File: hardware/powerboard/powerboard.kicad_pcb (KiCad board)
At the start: 4 copper layers, 81.2 x 50.7 mm, 73 parts, among them J1 USB_B_Micro, J10 5V, J11 3V3, J2 Boot, J3 Keysboard Header, J4 Display, J5 Debug, J7 UART_0, J8 I2C_0, J9 I2C_1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

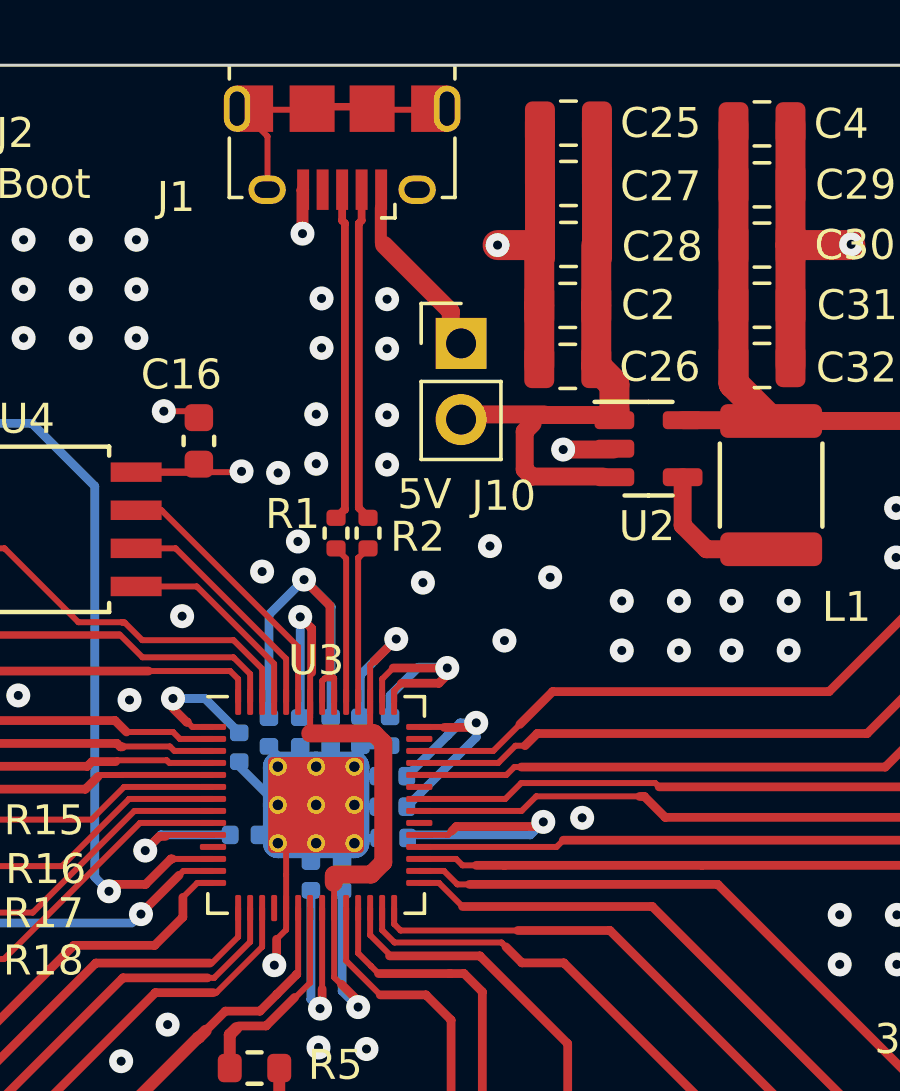
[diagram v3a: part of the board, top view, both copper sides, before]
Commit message: output file changes AND notes! Octave is now limited between 9 2 which corresponds to a piano range of C8 to C1, there are 3 notes below C1, that we will not be able to produce.
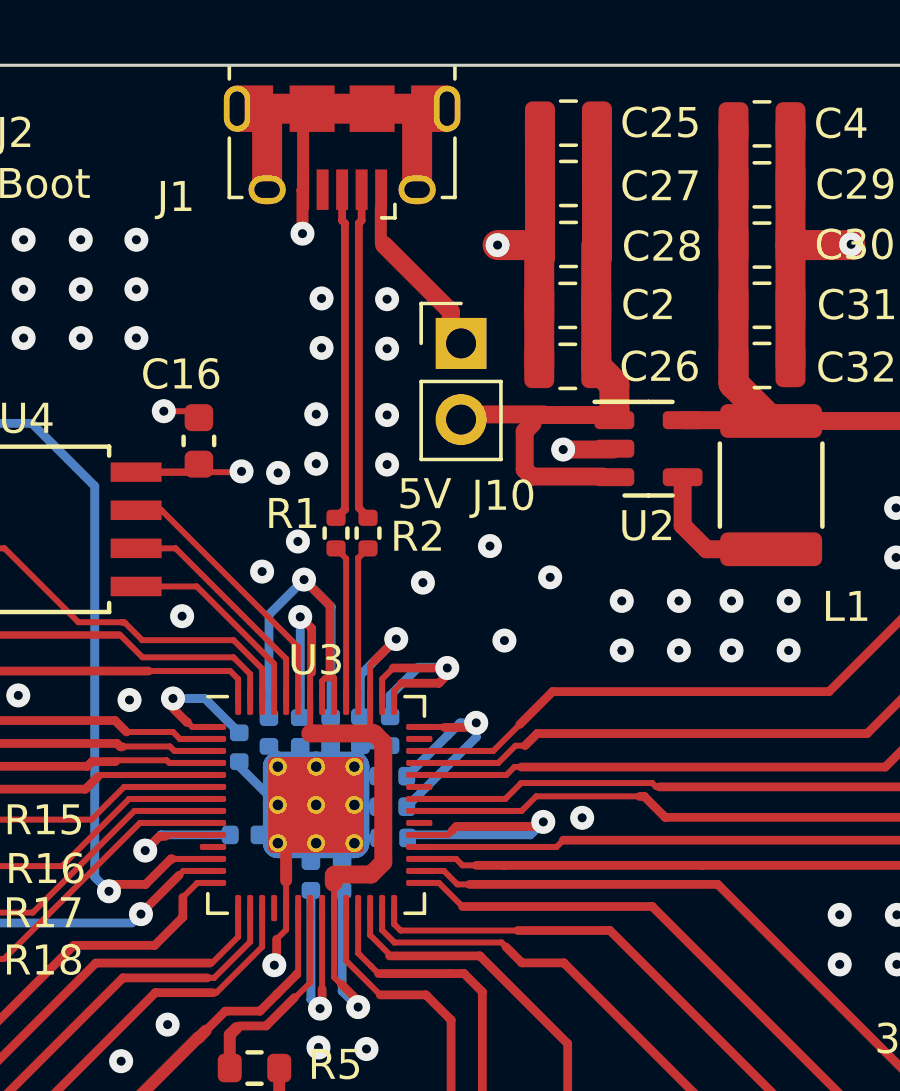
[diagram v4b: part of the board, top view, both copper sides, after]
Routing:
- net GND: track 105.7 -> 111.1 mm
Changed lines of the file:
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@@
     (effects (font (size 1 1) (thickness 0.15)))
   )
+  (segment (start 75.281 19.337) (end 75.281 16.937) (width 0.4) (layer "F.Cu") (net 1))
   (segment (start 58.6993 46.6344) (end 59.4613 47.3964) (width 0.2) (layer "F.Cu") (net 1))
+  (segment (start 75.581 16.637) (end 73.681 16.637) (width 1) (layer "F.Cu") (net 1))
   (segment (start 118.9494 37.374) (end 125.4494 37.374) (width 0.29337) (layer "F.Cu") (net 1))
   (segment (start 75.1722 53.6058) (end 75.184 53.594) (width 0.4) (layer "F.Cu") (net 1))
@@
   (segment (start 116.6244 56.1848) (end 116.6244 55.131) (width 0.29337) (layer "F.Cu") (net 1))
   (segment (start 99.5172 19.3294) (end 99.5172 19.203) (width 0.2) (layer "F.Cu") (net 1))
+  (segment (start 74.7144 43.28315) (end 74.7144 42.3672) (width 0.2) (layer "F.Cu") (net 1))
   (segment (start 83.17715 21.1632) (end 83.17715 19.1312) (width 1) (layer "F.Cu") (net 1))
   (segment (start 64.4652 32.4866) (end 64.389 32.5628) (width 0.2) (layer "F.Cu") (net 1))
@@
   (segment (start 74.3966 45.110004) (end 74.3458 45.160804) (width 0.29337) (layer "F.Cu") (net 1))
   (segment (start 58.2676 45.6184) (end 59.2581 45.6184) (width 0.2) (layer "F.Cu") (net 1))
+  (segment (start 74.081 17.037) (end 73.681 16.637) (width 1) (layer "F.Cu") (net 1))
   (segment (start 59.4613 44.2468) (end 58.6232 44.2468) (width 0.2) (layer "F.Cu") (net 1))
   (segment (start 75.2602 19.3528) (end 75.281 19.332) (width 0.4) (layer "F.Cu") (net 1))
-  (segment (start 74.7144 42.177) (end 74.7144 40.84565) (width 0.2) (layer "F.Cu") (net 1))
   (segment (start 74.7144 40.84565) (end 75.7144 39.84565) (width 0.2) (layer "F.Cu") (net 1))
-  (segment (start 77.731 16.672) (end 79.956 16.672) (width 0.2) (layer "F.Cu") (net 1))
+  (segment (start 74.7144 42.3672) (end 74.7144 40.84565) (width 0.4) (layer "F.Cu") (net 1))
   (segment (start 72.2884 50.2158) (end 72.263 50.2412) (width 0.4) (layer "F.Cu") (net 1))
   (segment (start 83.15175 21.1886) (end 83.17715 21.1632) (width 0.4) (layer "F.Cu") (net 1))
@@
   (segment (start 85.6285 27.99855) (end 85.65665 27.9704) (width 0.4) (layer "F.Cu") (net 1))
   (segment (start 74.3966 44.323) (end 74.7144 44.0052) (width 0.2) (layer "F.Cu") (net 1))
+  (segment (start 75.581 16.637) (end 77.581 16.637) (width 1) (layer "F.Cu") (net 1))
   (segment (start 125.7046 31.4452) (end 126.5454 31.4452) (width 0.25) (layer "F.Cu") (net 1))
   (segment (start 105.3084 29.6926) (end 105.3084 28.5978) (width 0.25) (layer "F.Cu") (net 1))
@@
   (segment (start 70.9552 51.5202) (end 70.9552 50.165) (width 0.4) (layer "F.Cu") (net 1))
   (segment (start 99.581 19.1392) (end 99.581 17.7292) (width 0.6) (layer "F.Cu") (net 1))
+  (segment (start 79.081 19.337) (end 79.081 17.037) (width 1) (layer "F.Cu") (net 1))
   (segment (start 74.3966 44.323) (end 74.3966 45.110004) (width 0.29337) (layer "F.Cu") (net 1))
   (segment (start 105.0798 20.574) (end 105.0798 21.183) (width 0.2) (layer "F.Cu") (net 1))
@@
   (segment (start 116.7006 38.6464) (end 116.7006 39.7002) (width 0.29337) (layer "F.Cu") (net 1))
   (segment (start 58.2422 43.4848) (end 58.6993 43.4848) (width 0.2) (layer "F.Cu") (net 1))
-  (segment (start 74.0935 19.247) (end 74.0935 17.5595) (width 0.2) (layer "F.Cu") (net 1))
   (segment (start 74.7144 44.0052) (end 74.7144 43.28315) (width 0.2) (layer "F.Cu") (net 1))
   (segment (start 75.2602 20.8026) (end 75.2602 19.3528) (width 0.4) (layer "F.Cu") (net 1))
   (segment (start 126.5454 31.4452) (end 127.0026 30.988) (width 0.25) (layer "F.Cu") (net 1))
   (segment (start 115.951 37.8968) (end 116.7006 38.6464) (width 0.29337) (layer "F.Cu") (net 1))
-  (segment (start 74.0935 17.5595) (end 73.206 16.672) (width 0.2) (layer "F.Cu") (net 1))
   (segment (start 83.15175 25.2272) (end 83.15175 23.1952) (width 1) (layer "F.Cu") (net 1))
   (segment (start 70.6374 26.7208) (end 71.9452 26.7208) (width 0.2) (layer "F.Cu") (net 1))
   (segment (start 116.6244 55.131) (end 116.1288 54.6354) (width 0.29337) (layer "F.Cu") (net 1))
-  (segment (start 75.581 16.572) (end 77.581 16.572) (width 0.25) (layer "F.Cu") (net 1))
+  (segment (start 77.581 16.637) (end 79.481 16.637) (width 1) (layer "F.Cu") (net 1))
   (segment (start 93.5228 21.1836) (end 93.5482 21.1582) (width 0.4) (layer "F.Cu") (net 1))
   (segment (start 85.60585 28.0212) (end 85.5832 27.99855) (width 0.4) (layer "F.Cu") (net 1))
@@
   (segment (start 71.3408 51.9058) (end 70.9552 51.5202) (width 0.4) (layer "F.Cu") (net 1))
   (segment (start 83.15175 23.1952) (end 83.15175 21.1886) (width 1) (layer "F.Cu") (net 1))
-  (segment (start 74.7144 43.28315) (end 74.7144 42.177) (width 0.2) (layer "F.Cu") (net 1))
   (segment (start 74.3458 45.160804) (end 74.320202 45.186402) (width 0.2) (layer "F.Cu") (net 1))
-  (segment (start 75.031 16.672) (end 73.206 16.672) (width 0.2) (layer "F.Cu") (net 1))
+  (segment (start 79.081 17.037) (end 79.481 16.637) (width 1) (layer "F.Cu") (net 1))
   (segment (start 99.5172 19.203) (end 99.581 19.1392) (width 0.2) (layer "F.Cu") (net 1))
+  (segment (start 75.281 16.937) (end 75.581 16.637) (width 0.4) (layer "F.Cu") (net 1))
   (segment (start 83.94935 27.99855) (end 85.6285 27.99855) (width 0.6) (layer "F.Cu") (net 1))
+  (segment (start 74.081 19.337) (end 74.081 17.037) (width 1) (layer "F.Cu") (net 1))
   (segment (start 83.1748 19.12885) (end 83.17715 19.1312) (width 0.4) (layer "F.Cu") (net 1))
   (segment (start 73.5408 53.6058) (end 75.1722 53.6058) (width 0.4) (layer "F.Cu") (net 1))
@@
   (segment (start 77.5144 43.28315) (end 77.5144 44.183886) (width 0.2) (layer "F.Cu") (net 7))
   (segment (start 85.7504 56.9976) (end 84.0994 55.3466) (width 0.29337) (layer "F.Cu") (net 7))
+  (segment (start 87.0458 39.243) (end 87.1474 39.243) (width 0.2) (layer "F.Cu") (net 8))
   (segment (start 114.6934 39.243) (end 115.1506 39.7002) (width 0.2) (layer "F.Cu") (net 8))
-  (segment (start 87.0204 39.116) (end 87.1474 39.243) (width 0.2) (layer "F.Cu") (net 8))
+  (segment (start 86.9188 39.116) (end 87.0458 39.243) (width 0.2) (layer "F.Cu") (net 8))
   (segment (start 115.1006 41.1734) (end 115.1006 39.7502) (width 0.29337) (layer "F.Cu") (net 8))
   (segment (start 115.1006 39.7502) (end 115.1506 39.7002) (width 0.2) (layer "F.Cu") (net 8))
+  (segment (start 87.1474 39.243) (end 114.6934 39.243) (width 0.29337) (layer "F.Cu") (net 8))
   (segment (start 79.1519 39.64565) (end 82.02035 39.64565) (width 0.2) (layer "F.Cu") (net 8))
-  (segment (start 87.1474 39.243) (end 114.6934 39.243) (width 0.29337) (layer "F.Cu") (net 8))
-  (segment (start 82.55 39.116) (end 87.0204 39.116) (width 0.2) (layer "F.Cu") (net 8))
   (segment (start 82.02035 39.64565) (end 82.55 39.116) (width 0.2) (layer "F.Cu") (net 8))
+  (segment (start 82.55 39.116) (end 86.9188 39.116) (width 0.2) (layer "F.Cu") (net 8))
   (segment (start 77.4446 30.2514) (end 77.4446 30.2748) (width 0.261112) (layer "F.Cu") (net 9))
   (segment (start 77.231 20.367001) (end 77.138156 20.459845) (width 0.261112) (layer "F.Cu") (net 9))

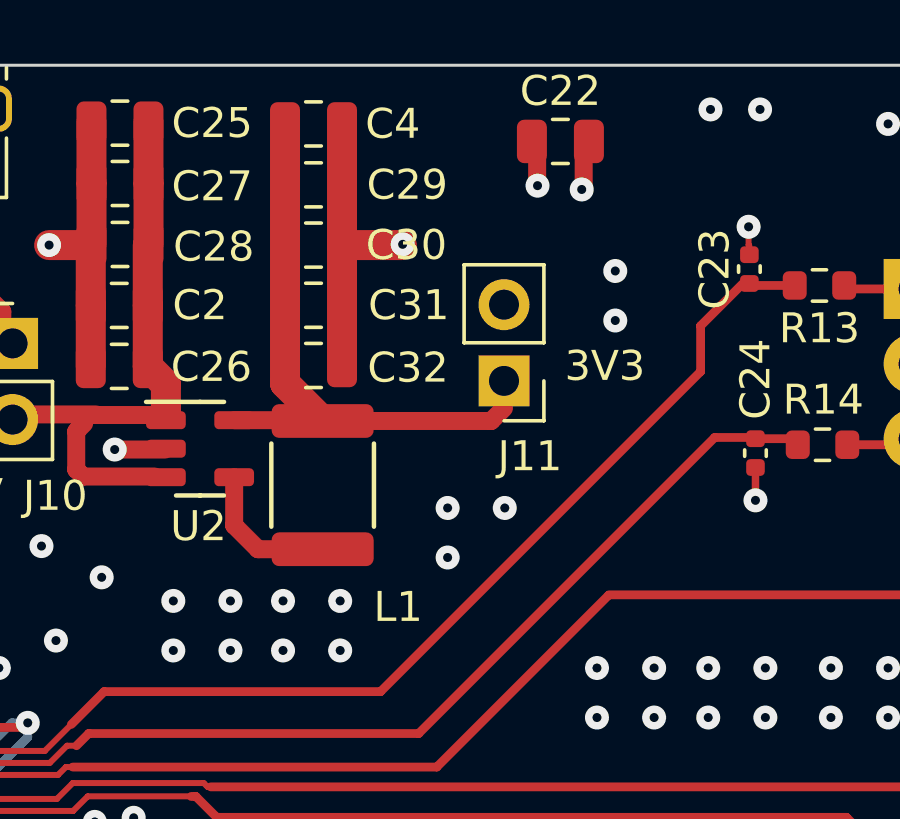
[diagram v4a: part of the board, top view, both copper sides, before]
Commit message: Everything but Keysboard and Display tested.
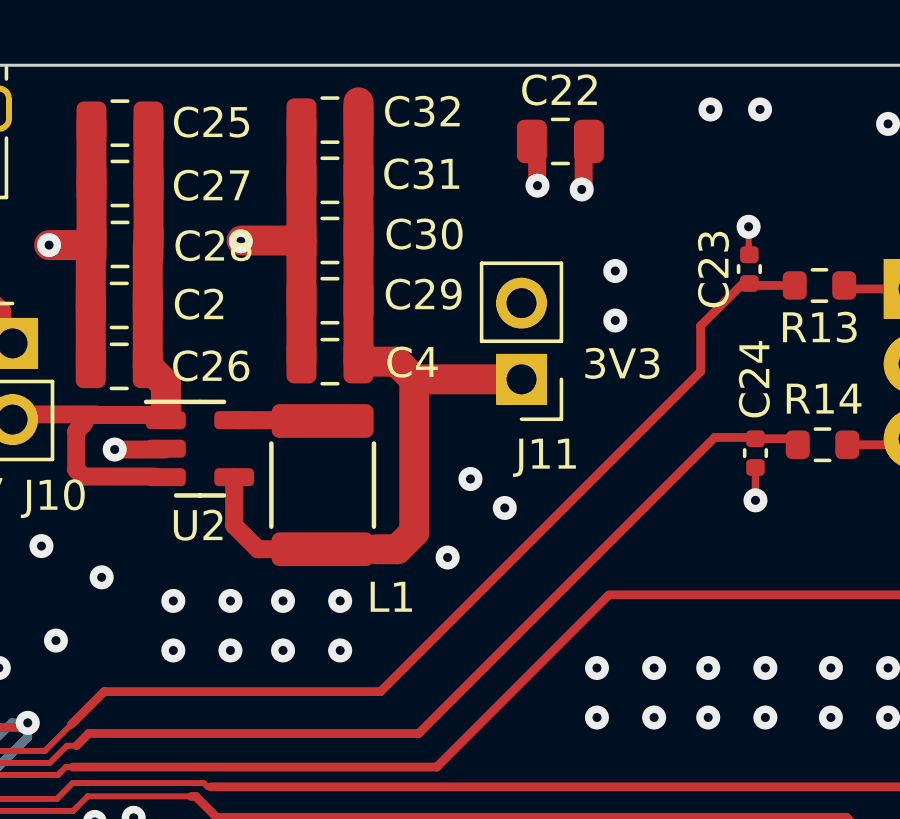
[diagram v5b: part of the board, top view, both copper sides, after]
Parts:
- moved C32 8.20 mm to (91.1, 17.0), turned to 180 degrees
- moved C4 7.94 mm to (91.1, 25.1), turned to 180 degrees
- moved C31 4.20 mm to (91.1, 19.0), turned to 180 degrees
- moved C29 3.90 mm to (91.1, 23.0), turned to 180 degrees
- moved J11 0.59 mm to (97.5, 25.7)
- moved C30 0.57 mm to (91.1, 21.0), turned to 180 degrees
- turned L1 to -90 degrees
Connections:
- U2 pad 4: Net-(L1-Pad1) -> VDD
- U2 pad 5: VDD -> Net-(L1-Pad1)
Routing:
- net VDD: track 20.5 -> 24.1 mm
- net Net-(L1-Pad1): track 4.89 -> 2.96 mm

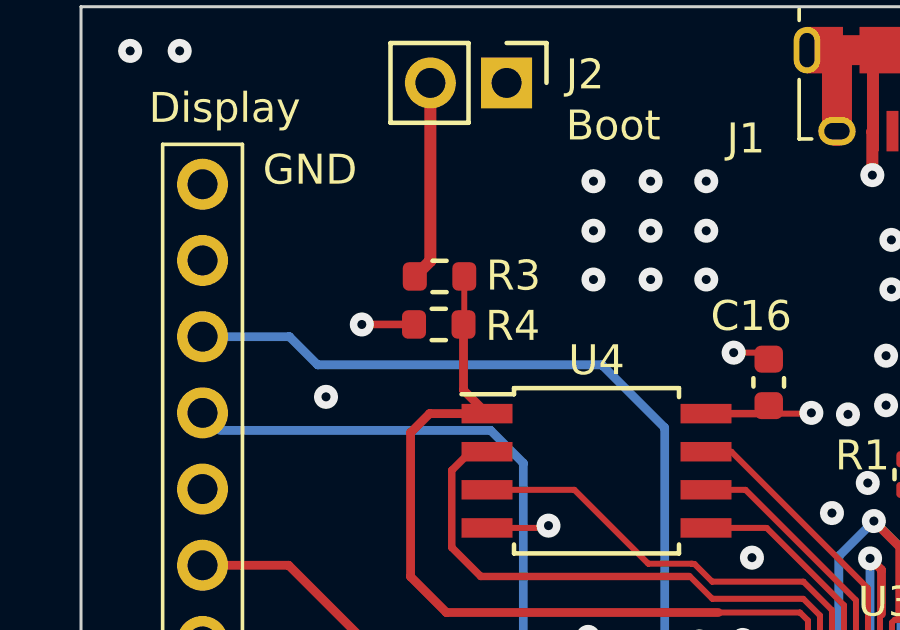
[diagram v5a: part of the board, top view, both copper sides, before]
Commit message: Powerboard REV2 - R4 Removed
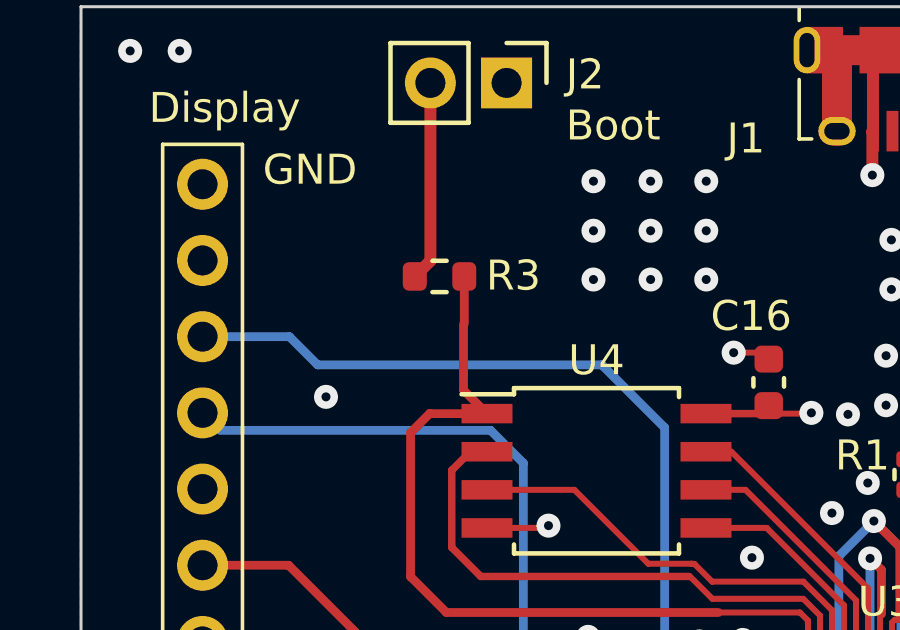
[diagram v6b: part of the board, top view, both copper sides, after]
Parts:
- removed R4: 10k, Resistor_SMD:R_0603_1608Metric
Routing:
- net +3.3V: track 72.1 -> 70.3 mm, vias 13 -> 12
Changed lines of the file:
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@@
-    )
-  )
-  (footprint "Resistor_SMD:R_0603_1608Metric" (layer "F.Cu")
-    (at 60.8076 25.781)
-    (descr "Resistor SMD 0603 (1608 Metric), square (rectangular) end terminal, IPC_7351 nominal, (Body size source: IPC-SM-782 page 72, https://www.pcb-3d.com/wordpress/wp-content/uploads/ipc-sm-782a_amendment_1_and_2.pdf), generated with kicad-footprint-generator")
-    (tags "resistor")
-    (property "LCSC" "C25804")
-    (property "Sheetfile" "File: powerboard.kicad_sch")
-    (property "Sheetname" "")
-    (attr smd)
-    (fp_text reference "R4" (at 2.4638 0.0508 unlocked) (layer "F.SilkS")
-      (effects (font (size 1 1) (thickness 0.15)))
-    )
-    (fp_text value "10k" (at 0 1.43 unlocked) (layer "F.Fab") hide
-      (effects (font (size 1 1) (thickness 0.15)))
-    )
-    (fp_text user "${REFERENCE}" (at -0.0762 -0.0254 unlocked) (layer "F.Fab") hide
-      (effects (font (size 1 1) (thickness 0.15)))
-    )
-    (fp_line (start -0.237258 0.5225) (end 0.237258 0.5225) (layer "F.SilkS") (width 0.15))
-    (fp_line (start -0.237258 -0.5225) (end 0.237258 -0.5225) (layer "F.SilkS") (width 0.15))
-    (fp_line (start 1.48 0.73) (end -1.48 0.73) (layer "F.CrtYd") (width 0.05))
-    (fp_line (start -1.48 -0.73) (end 1.48 -0.73) (layer "F.CrtYd") (width 0.05))
-    (fp_line (start -1.48 0.73) (end -1.48 -0.73) (layer "F.CrtYd") (width 0.05))
-    (fp_line (start 1.48 -0.73) (end 1.48 0.73) (layer "F.CrtYd") (width 0.05))
-    (fp_line (start -0.8 0.4125) (end -0.8 -0.4125) (layer "F.Fab") (width 0.1))
-    (fp_line (start 0.8 0.4125) (end -0.8 0.4125) (layer "F.Fab") (width 0.1))
-    (fp_line (start 0.8 -0.4125) (end 0.8 0.4125) (layer "F.Fab") (width 0.1))
-    (fp_line (start -0.8 -0.4125) (end 0.8 -0.4125) (layer "F.Fab") (width 0.1))
-    (pad "1" smd roundrect (at -0.825 0) (size 0.8 0.95) (layers "F.Cu" "F.Paste" "F.Mask") (roundrect_rratio 0.25)
-      (net 2 "+3.3V") (pintype "passive"))
-    (pad "2" smd roundrect (at 0.825 0) (size 0.8 0.95) (layers "F.Cu" "F.Paste" "F.Mask") (roundrect_rratio 0.25)
-      (net 20 "/QSPI_SS") (pintype "passive"))
-    (model "${KICAD6_3DMODEL_DIR}/Resistor_SMD.3dshapes/R_0603_1608Metric.wrl"
-      (offset (xyz 0 0 0))
-      (scale (xyz 1 1 1))
-      (rotate (xyz 0 0 0))
     )
   )
@@
   (segment (start 77.16525 40.9448) (end 76.9894 41.12065) (width 0.25) (layer "B.Cu") (net 1))
   (segment (start 79.8068 35.7886) (end 80.0862 35.5092) (width 0.29337) (layer "F.Cu") (net 2))
-  (segment (start 59.9826 25.781) (end 58.2422 25.781) (width 0.254254) (layer "F.Cu") (net 2))
   (segment (start 98.031 19.1894) (end 98.031 17.7292) (width 0.6) (layer "F.Cu") (net 2))
   (segment (start 75.311 32.3342) (end 76.1746 33.1978) (width 0.29337) (layer "F.Cu") (net 2))
@@
   (via (at 98.044 19.2024) (size 0.8) (drill 0.3) (layers "F.Cu" "B.Cu") (free) (net 2))
   (via (at 75.311 32.3342) (size 0.8) (drill 0.3) (layers "F.Cu" "B.Cu") (free) (net 2))
-  (via (at 58.2422 25.781) (size 0.8) (drill 0.3) (layers "F.Cu" "B.Cu") (net 2))
   (segment (start 75.311 32.3342) (end 74.1426 33.5026) (width 0.29337) (layer "B.Cu") (net 2))
   (segment (start 80.518 37.1094) (end 81.0514 37.1094) (width 0.29337) (layer "B.Cu") (net 2))
@@
   (segment (start 73.1144 35.6484) (end 72.8482 35.3822) (width 0.2) (layer "F.Cu") (net 20))
   (segment (start 72.8482 35.3822) (end 70.1294 35.3822) (width 0.2) (layer "F.Cu") (net 20))
-  (segment (start 61.658 24.1808) (end 61.658 25.7556) (width 0.2) (layer "F.Cu") (net 20))
+  (segment (start 61.658 24.1808) (end 61.658 25.7556) (width 0.29337) (layer "F.Cu") (net 20))
   (segment (start 61.0616 35.3822) (end 59.8678 34.1884) (width 0.29337) (layer "F.Cu") (net 20))
   (segment (start 60.5028 28.7528) (end 62.4154 28.7528) (width 0.29337) (layer "F.Cu") (net 20))
